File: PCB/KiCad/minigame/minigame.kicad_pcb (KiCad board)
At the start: 2 copper layers, 100 x 100 mm, 13 parts, among them J1 Conn_01x04_Pin, SW1 SW_Push, SW2 SW_Push, SW3 SW_Push, SW4 SW_Push, SW5 SW_Push, SW6 SW_Push

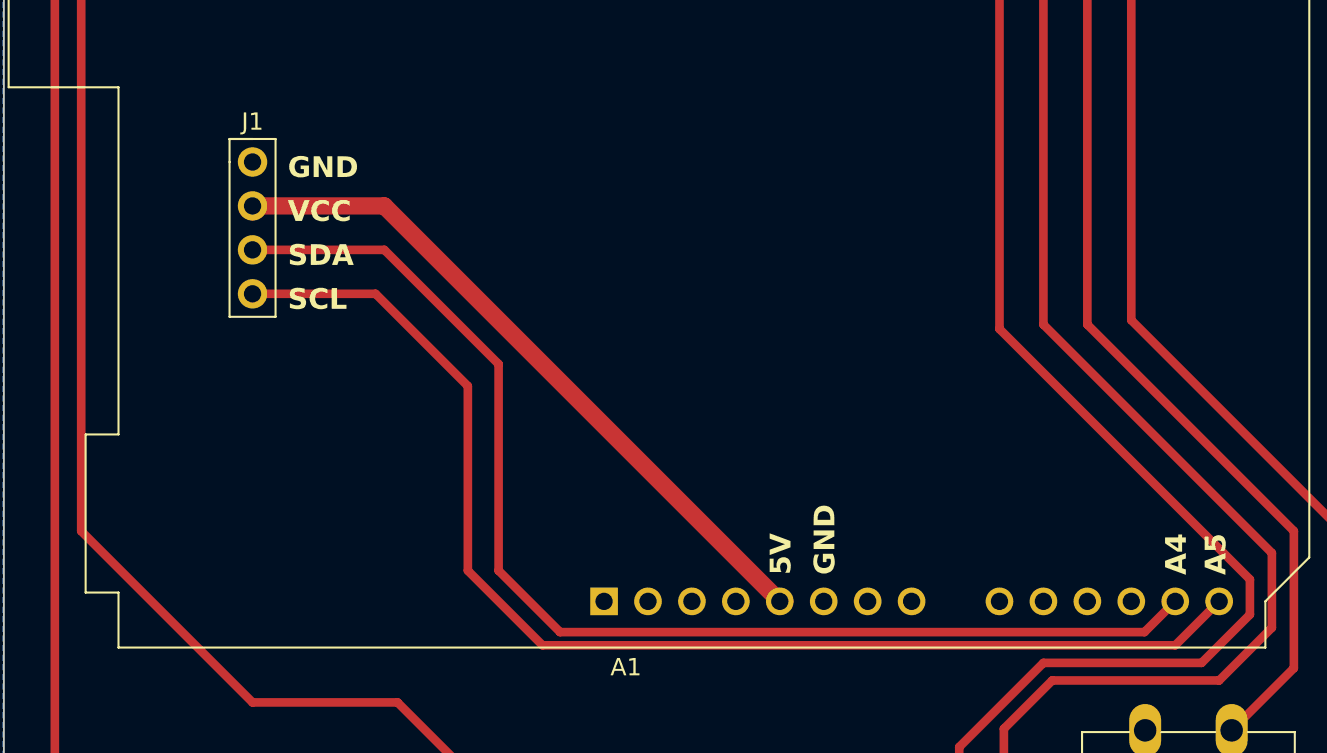
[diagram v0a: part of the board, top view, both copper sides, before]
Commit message: feat: added 3D model and updated the PCB
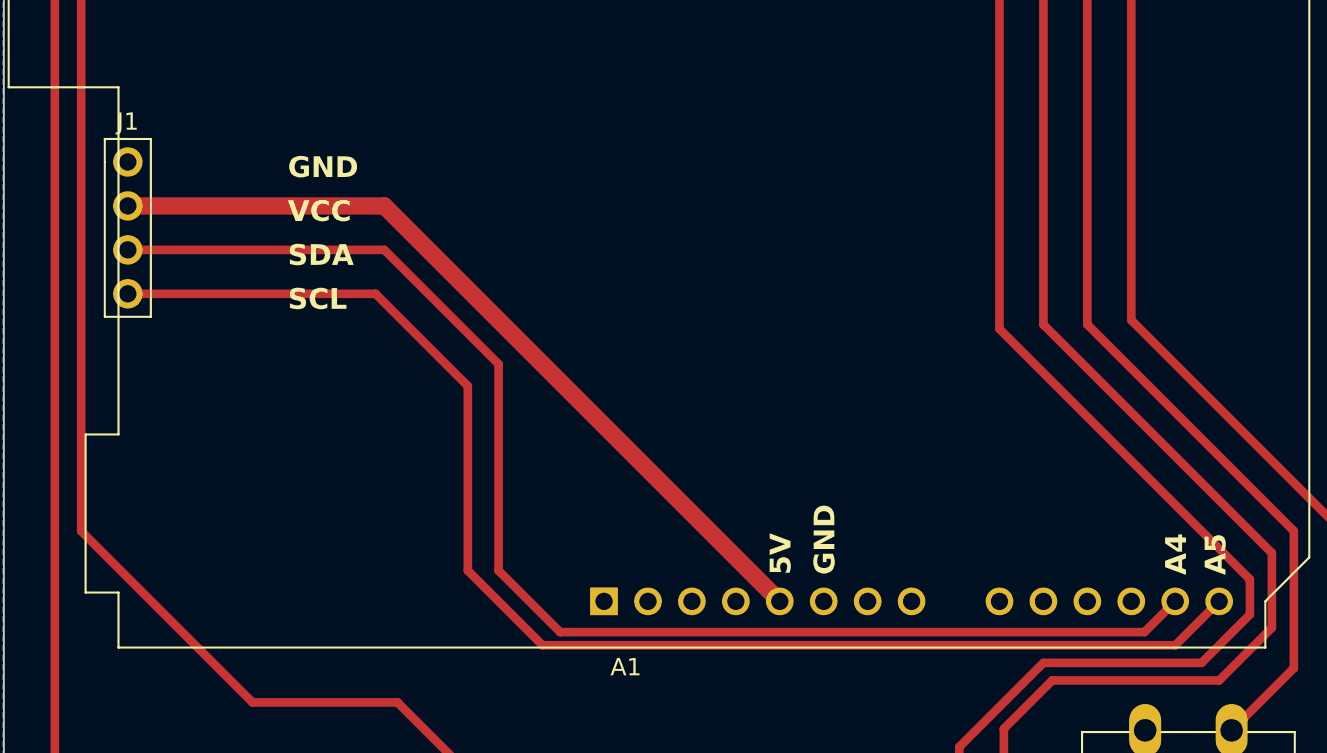
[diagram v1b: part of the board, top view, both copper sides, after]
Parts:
- moved J1 7.21 mm to (91.8, 76.2)
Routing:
- net /SDA: track 70.2 -> 77.4 mm
- net /SCL: track 71.6 -> 78.8 mm
- net +5V: track 39.9 -> 47.2 mm
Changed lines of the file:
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@@
   )
   (footprint "Connector_PinHeader_2.54mm:PinHeader_1x04_P2.54mm_Vertical" (layer "F.Cu")
-    (at 99.06 76.2)
+    (at 91.85 76.2)
     (descr "Through hole straight pin header, 1x04, 2.54mm pitch, single row")
     (tags "Through hole pin header THT 1x04 2.54mm single row")
@@
     (effects (font (size 1.2 1.2) (thickness 0.3) bold) (justify left bottom))
   )
-  (segment (start 99.06 78.74) (end 106.68 78.74) (width 1) (layer "F.Cu") (net 5))
-  (segment (start 106.68 78.74) (end 129.54 101.6) (width 1) (layer "F.Cu") (net 5))
-  (segment (start 99.06 81.28) (end 106.68 81.28) (width 0.5) (layer "F.Cu") (net 12))
-  (segment (start 150.622 103.378) (end 152.4 101.6) (width 0.5) (layer "F.Cu") (net 12))
-  (segment (start 113.284 87.884) (end 113.284 99.822) (width 0.5) (layer "F.Cu") (net 12))
-  (segment (start 106.68 81.28) (end 113.284 87.884) (width 0.5) (layer "F.Cu") (net 12))
-  (segment (start 116.84 103.378) (end 150.622 103.378) (width 0.5) (layer "F.Cu") (net 12))
-  (segment (start 113.284 99.822) (end 116.84 103.378) (width 0.5) (layer "F.Cu") (net 12))
-  (segment (start 115.824 104.14) (end 152.4 104.14) (width 0.5) (layer "F.Cu") (net 13))
-  (segment (start 99.06 83.82) (end 106.172 83.82) (width 0.5) (layer "F.Cu") (net 13))
-  (segment (start 152.4 104.14) (end 154.94 101.6) (width 0.5) (layer "F.Cu") (net 13))
-  (segment (start 106.172 83.82) (end 111.506 89.154) (width 0.5) (layer "F.Cu") (net 13))
-  (segment (start 111.506 89.154) (end 111.506 99.822) (width 0.5) (layer "F.Cu") (net 13))
-  (segment (start 111.506 99.822) (end 115.824 104.14) (width 0.5) (layer "F.Cu") (net 13))
+  (segment (start 129.54 101.6) (end 106.68 78.74) (width 1) (layer "F.Cu") (net 5))
+  (segment (start 106.68 78.74) (end 91.85 78.74) (width 1) (layer "F.Cu") (net 5))
+  (segment (start 150.622 103.378) (end 116.84 103.378) (width 0.5) (layer "F.Cu") (net 12))
+  (segment (start 113.284 87.884) (end 106.68 81.28) (width 0.5) (layer "F.Cu") (net 12))
+  (segment (start 113.284 99.822) (end 113.284 87.884) (width 0.5) (layer "F.Cu") (net 12))
+  (segment (start 106.68 81.28) (end 91.85 81.28) (width 0.5) (layer "F.Cu") (net 12))
+  (segment (start 116.84 103.378) (end 113.284 99.822) (width 0.5) (layer "F.Cu") (net 12))
+  (segment (start 152.4 101.6) (end 150.622 103.378) (width 0.5) (layer "F.Cu") (net 12))
+  (segment (start 111.506 99.822) (end 111.506 89.154) (width 0.5) (layer "F.Cu") (net 13))
+  (segment (start 106.172 83.82) (end 91.85 83.82) (width 0.5) (layer "F.Cu") (net 13))
+  (segment (start 154.94 101.6) (end 152.4 104.14) (width 0.5) (layer "F.Cu") (net 13))
+  (segment (start 152.4 104.14) (end 115.824 104.14) (width 0.5) (layer "F.Cu") (net 13))
+  (segment (start 115.824 104.14) (end 111.506 99.822) (width 0.5) (layer "F.Cu") (net 13))
+  (segment (start 111.506 89.154) (end 106.172 83.82) (width 0.5) (layer "F.Cu") (net 13))
   (segment (start 149.86 85.344) (end 171.664 107.148) (width 0.5) (layer "F.Cu") (net 16))
   (segment (start 171.664 120.232) (end 171.664 132.732) (width 0.5) (layer "F.Cu") (net 16))
